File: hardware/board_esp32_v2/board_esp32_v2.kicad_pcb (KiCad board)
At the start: 2 copper layers, 55 x 80 mm, 96 parts, among them J1 USB_B_Micro, J2 Conn_01x02, J3 Micro_SD_Card_Det_Hirose_DM3AT, Q1 AO3401, Q2 AO3400, Q3 AO3401, SW1 SW_Push-Std, U1 FT231XS, U2 ESP32-WROOM-32D, U3 E22-900M22S, U4 E22-900M30S, U5 TPS62162DGK

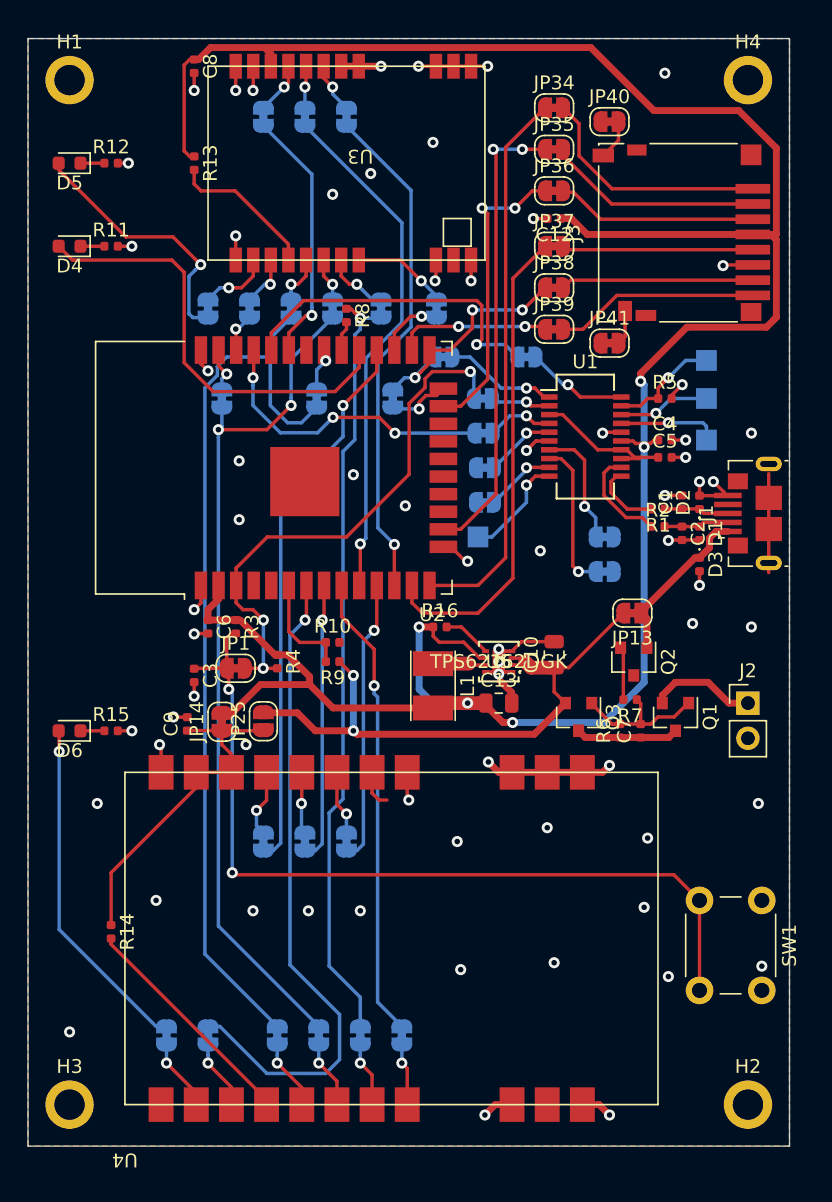
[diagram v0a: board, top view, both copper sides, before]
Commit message: Finish implementing fixes and pin changes for board_esp32_v2.
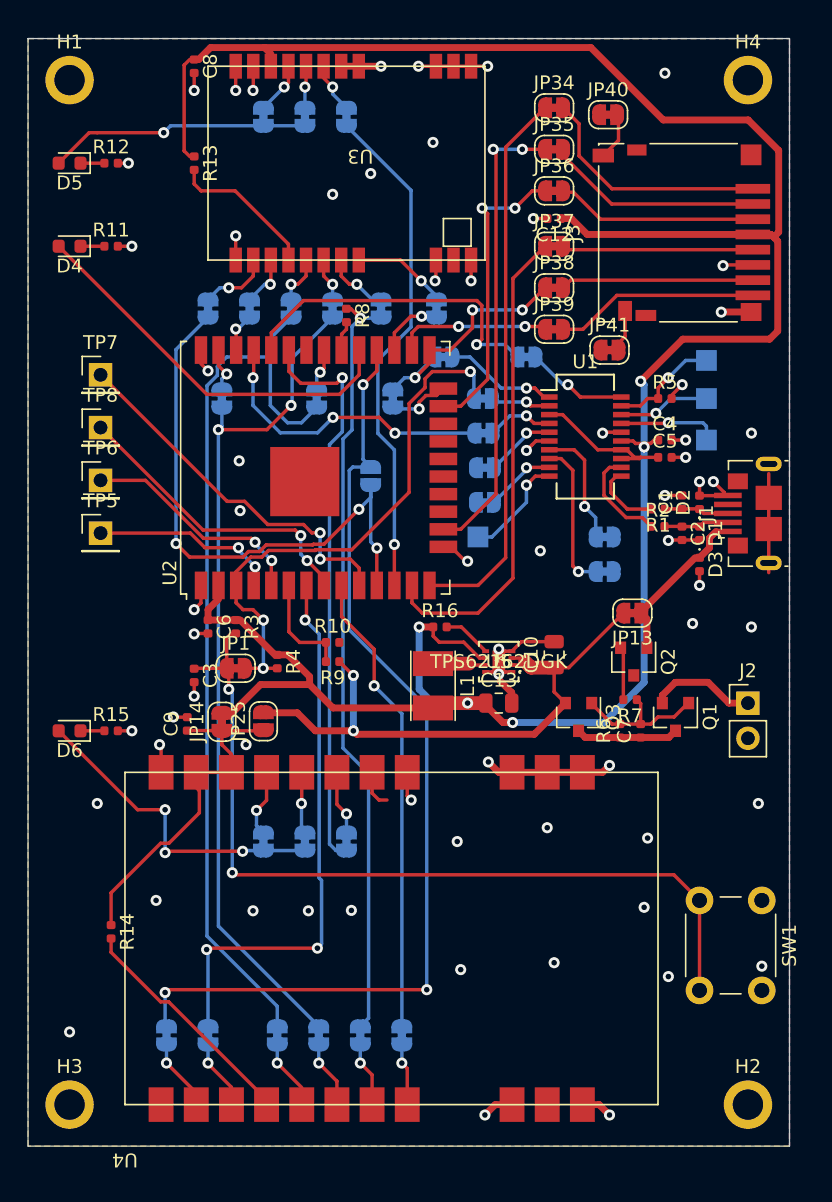
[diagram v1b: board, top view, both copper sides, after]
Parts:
- added JP42: SolderJumper_2_Open, Jumper:SolderJumper-2_P1.3mm_Open_RoundedPad1.0x1.5mm, B.Cu at (34.8, 41.6)
- added TP5: TP_HOLE, Connector_PinHeader_2.54mm:PinHeader_1x01_P2.54mm_Vertical, F.Cu at (15.2, 45.7)
- added TP6: TP_HOLE, Connector_PinHeader_2.54mm:PinHeader_1x01_P2.54mm_Vertical, F.Cu at (15.2, 41.9)
- added TP7: TP_HOLE, Connector_PinHeader_2.54mm:PinHeader_1x01_P2.54mm_Vertical, F.Cu at (15.2, 34.3)
- added TP8: TP_HOLE, Connector_PinHeader_2.54mm:PinHeader_1x01_P2.54mm_Vertical, F.Cu at (15.2, 38.1)
- R7: value 1K -> 100
- U2: value ESP32-WROOM-32D -> ESP32-WROOM-32U; footprint RF_Module:ESP32-WROOM-32 -> RF_Module:ESP32-WROOM-32U
- moved JP40 0.51 mm to (51.9, 15.5)
- moved JP41 0.50 mm to (52.0, 32.5)
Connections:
- D5 pad 2: /LORA1_DIO1 -> /LORA1_DIO2
- D6 pad 2: /LORA2_DIO1 -> /LORA2_DIO2
- JP16 pad 1: /LORA1_TXEN -> /LORA1_DIO2
- JP21 pad 1: /LORA2_TXEN -> /LORA2_DIO2
- U2 pad 10: /LORA1_TXEN -> Net-(TP7-Pad1)
- U2 pad 11: /LORA2_RXEN -> /LORA1_DIO1
- U2 pad 28: /LORA2_DIO2 -> /LORA2_DIO1
- U2 pad 33: /LORA1_DIO2 -> /LORA2_RXEN
- U2 pad 8: /LORA2_TXEN -> Net-(TP8-Pad1)
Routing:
- net /LORA2_DIO1: track 25.0 -> 72.9 mm, vias 1 -> 3
- net /LORA1_TXEN: track 37.4 -> 0.00 mm, vias 1 -> 0
- net Net-(TP7-Pad1): track 0.00 -> 26.8 mm, vias 0 -> 2
- net /LORA1_DIO1: track 19.0 -> 41.9 mm, vias 1 -> 3
- net Net-(TP8-Pad1): track 0.00 -> 22.0 mm, vias 0 -> 2
- net /LORA2_RXEN: track 20.5 -> 41.4 mm
- net /LORA2_TXEN: track 20.2 -> 0.00 mm, vias 1 -> 0
- net /LORA2_DIO2: track 40.0 -> 23.3 mm, vias 1 -> 3
- net Net-(TP6-Pad1): track 0.00 -> 16.6 mm, vias 0 -> 2
- net Net-(TP5-Pad1): track 0.00 -> 13.7 mm, vias 0 -> 2
- net /LORA2_BUSY: track 47.5 -> 40.5 mm, vias 1 -> 3
- net +3V3: track 181.1 -> 177.4 mm
- net /ESP_LED: track 31.9 -> 28.5 mm
- net /VBUS: track 11.8 -> 9.98 mm
- net /SW_RESET: track 61.3 -> 60.0 mm
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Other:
- net class Default removed
- net class PWR removed
